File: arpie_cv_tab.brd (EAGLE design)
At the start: 35.9 x 58.4 mm, 44 parts, among them IC1 MCP4726, IC2 74HC14D

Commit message: v2 board
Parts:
- added C10, C5: (no value), resistor:C0805
- added C6: (no value), rcl:SMC_A
- added C7, C8: 10u, rcl:SMC_A
- added D1: MBR0520LT, diode:SOD123
- added IC3: LM27675M5_CHARGEPUMP, jason_eagle6:SOT23-6
- added IC4: LM358D, linear:SO08
- added R1, R2, R3, R4, R5: (no value), rcl:R0805
- added R13: 1K, rcl:R0805
- IC2: value 74HC14D -> MCP601OT; device 74xx-eu:SO14 -> linear:SOT23-5
- R11, R12, R8: value 10K -> (none)
- R6, R7, R9: value 1K -> (none)
- moved R11 43.9 mm to (79.4, 8.89), turned to 270 degrees
- moved R12 32.4 mm to (81.9, 8.89), turned to 90 degrees
- moved IC2 25.4 mm to (71.1, 36.8)
- moved C2 22.9 mm to (71.1, 40.6)
- moved R6 15.5 mm to (63.5, 12.7), turned to 270 degrees
- moved R8 13.7 mm to (79.4, 16.1), turned to 90 degrees
- moved R7 12.7 mm to (66.0, 12.7), turned to 90 degrees
- moved IC1 11.0 mm to (66.0, 36.8), turned to 90 degrees
- moved C1 10.6 mm to (66.0, 40.6), turned to 180 degrees
- moved R10 10.3 mm to (84.5, 16.1), turned to 90 degrees
- moved C3 9.44 mm to (76.2, 36.8), turned to 180 degrees
- moved CLK_LED 7.62 mm to (88.9, 8.89)
- moved GATE_LED 7.62 mm to (88.9, 16.5)
- moved R9 3.30 mm to (81.9, 16.1), turned to 270 degrees
- moved C4 3.24 mm to (81.9, 29.2), turned to 180 degrees
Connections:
- removed net N$13: IC2.13, R9.2
- removed net N$14: IC2.3, R6.2
- removed net N$6: GATE_LED.A, R10.2
- removed net N$7: IC1.1, R11.1
- removed net N$8: CLK_LED.A, R7.2
- new net +10V: C10.1, C2.2, C6.+, D1.C, IC2.5, IC3.5, IC4.8
- new net CVOUT: CVOUT.T, CVOUT.T@, R1.1, R3.1
- new net DACOUT: IC1.1, IC2.3
- new net N$11: C3.2, IC2.1, R1.2
- new net N$15: C3.1, IC2.4, R2.1, R3.2
- new net N$38: C8.+, IC3.6
- new net N$39: C8.-, IC3.3
- net +5V: now also C1.2, C7.+, D1.A, IC3.1, R6.2; no longer C1.1, C2.2, IC2.14
- net CLK_OUT: now also CLK_LED.A, R12.2; no longer R9.1
- net GATE_OUT: now also GATE_LED.A, R9.2; no longer R6.1
- net GND: now also C1.1, C10.2, C5.2, C6.-, C7.-, GND1.1, GND2.1, GND3.1, GND4.1, GND5.1, GND6.1, IC2.2, IC3.2, IC3.4, IC4.4, R10.2, R13.2, R2.2, R7.1; no longer C1.2, C3.2, CLK_LED.K, GATE_LED.K, IC2.7
- net N$1: now also IC4.2, IC4.6, R6.1, R7.2; no longer CVOUT.T, CVOUT.T@, R11.2
- net N$12: now also IC4.7, R4.1, R8.1; no longer IC2.6, R12.1
- net N$19: now also C5.1, R5.2; no longer C4.1, R8.2
- net N$2: now also CLK_LED.K, R13.1; no longer IC2.8, R10.1
- net N$20: now also C4.1, R4.2; no longer C3.1, R12.2
- net N$3: now also GATE_LED.K, R10.1; no longer IC2.10, R7.1
- net N$4: now also IC4.3, R11.2, R12.1; no longer IC2.1, IC2.11, IC2.12
- net N$5: now also IC4.5, R8.2, R9.1; no longer IC2.4, IC2.5, IC2.9
- net N$9: now also IC4.1, R11.1, R5.1; no longer IC2.2, R8.1
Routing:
- net +10V: track 0.00 -> 46.7 mm, vias 0 -> 2
- net CVOUT: track 0.00 -> 34.6 mm
- net +5V: track 52.8 -> 86.4 mm, vias 2 -> 0
- net N$7: track 26.5 -> 0.00 mm
- net SDA: track 32.2 -> 55.2 mm, vias 1 -> 2
- net SCL: track 29.6 -> 51.9 mm, vias 1 -> 2
- net N$12: track 51.1 -> 32.3 mm
- net N$14: track 18.6 -> 0.00 mm, vias 2 -> 0
- net N$15: track 0.00 -> 11.6 mm
- net N$1: track 16.2 -> 27.3 mm, vias 0 -> 3
- net N$8: track 10.2 -> 0.00 mm
- net N$11: track 0.00 -> 10.2 mm
- net N$6: track 9.21 -> 0.00 mm
- net N$9: track 32.3 -> 24.1 mm, vias 0 -> 2
- net N$38: track 0.00 -> 6.48 mm
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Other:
- board text added: "/arpie"
- board text added: "V2"
- board text added: "six4pix.com"
- board text removed: "CLK"
- board text removed: "GTE"
- board text removed: "hotchk155"
- board text removed: "rev 1"

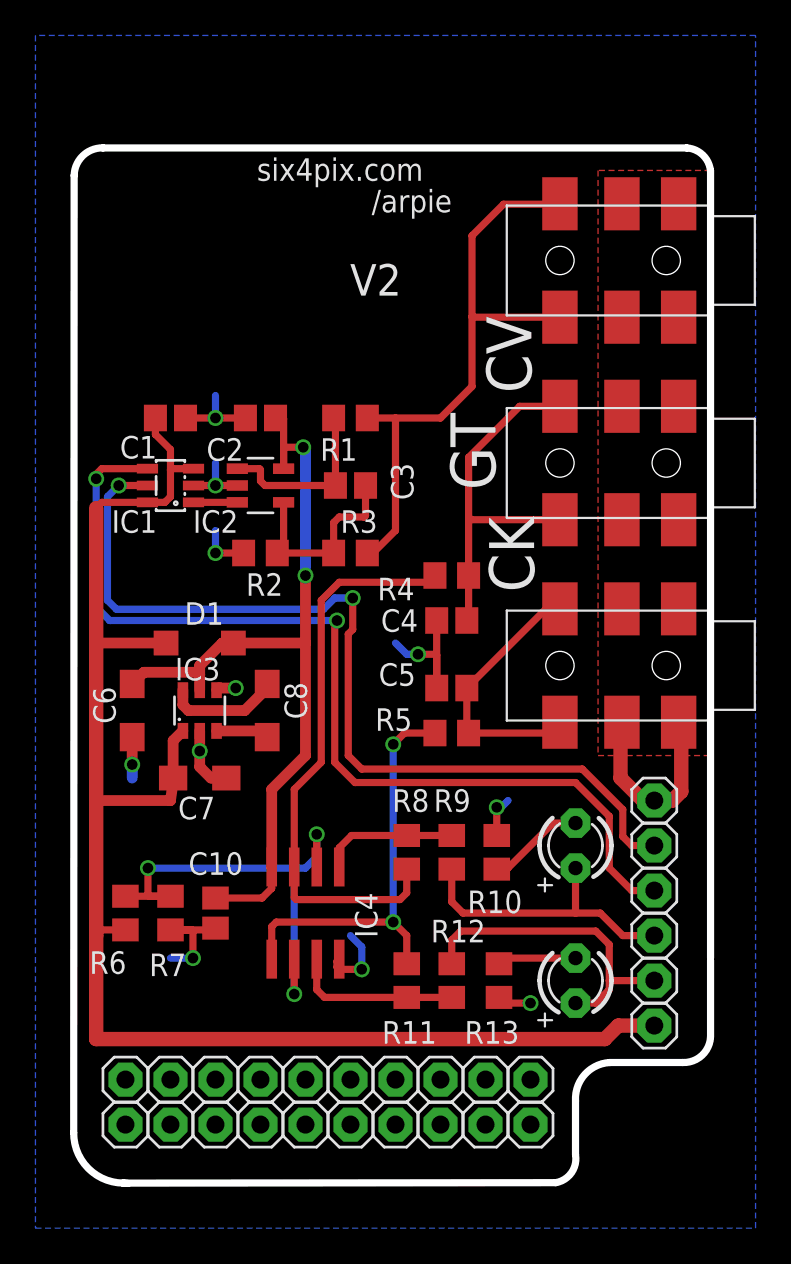
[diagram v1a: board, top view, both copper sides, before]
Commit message: v3 board
add voltage reference
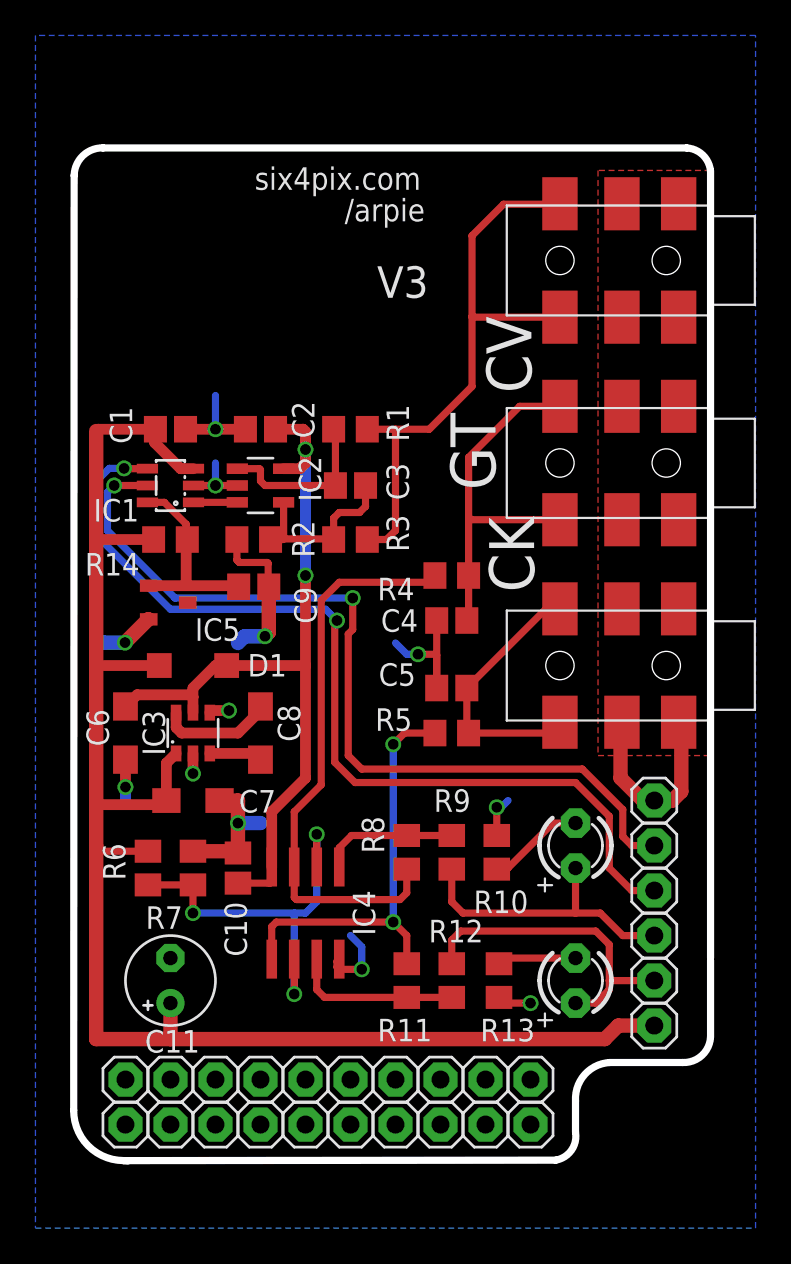
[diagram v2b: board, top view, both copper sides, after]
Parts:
- added C11: (no value), rcl:E2,5-5
- added C9: (no value), resistor:C0805
- added IC5: LM4041A12DBZ, texas:DBZ_R-PDSO-G3
- added R14: 3k, rcl:R0805
- R12, R6, R9: value (none) -> 100k
- moved C10 2.84 mm to (69.8, 15.2), turned to 90 degrees
- moved R6 2.84 mm to (64.8, 15.2), turned to 90 degrees
- moved R7 2.84 mm to (67.3, 15.2), turned to 270 degrees
- moved C6 1.33 mm to (63.5, 22.9)
- moved C7 1.33 mm to (67.3, 19.1)
- moved C8 1.33 mm to (71.1, 22.9)
- moved D1 1.33 mm to (67.3, 26.7)
- moved IC3 1.33 mm to (67.3, 22.9)
- moved R2 0.85 mm to (70.7, 33.8)
- moved R3 0.76 mm to (76.2, 33.8)
- moved C1 0.63 mm to (66.0, 40.0)
- moved C2 0.63 mm to (71.1, 40.0)
- moved R1 0.63 mm to (76.2, 40.0)
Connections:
- new net N$6: C9.2, IC1.6, IC5.1, R14.1
- net +5V: now also C11.+, R14.2; no longer IC1.6
- net GND: now also C11.-, C9.1, IC5.2
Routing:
- net N$6: track 0.00 -> 11.4 mm
- net GND: track 54.7 -> 63.0 mm, vias 11 -> 12
- net +5V: track 86.4 -> 92.5 mm
- net SCL: track 51.9 -> 49.3 mm
- net SDA: track 55.2 -> 52.6 mm
- net N$1: track 27.3 -> 24.8 mm
- net +10V: track 46.7 -> 44.4 mm
- net N$15: track 11.6 -> 10.1 mm
- net CVOUT: track 34.6 -> 33.6 mm
- net N$11: track 10.2 -> 9.52 mm
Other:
- board size 35.9 x 58.4 mm -> 35.9 x 57.2 mm
- board text added: "V3"
- board text removed: "V2"
